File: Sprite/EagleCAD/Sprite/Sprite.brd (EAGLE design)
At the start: 35 x 35 mm, 29 parts, among them U1 CC430F5137, U2 HMC5883LSMD, U3 ITG-3200, X1 26 MHz

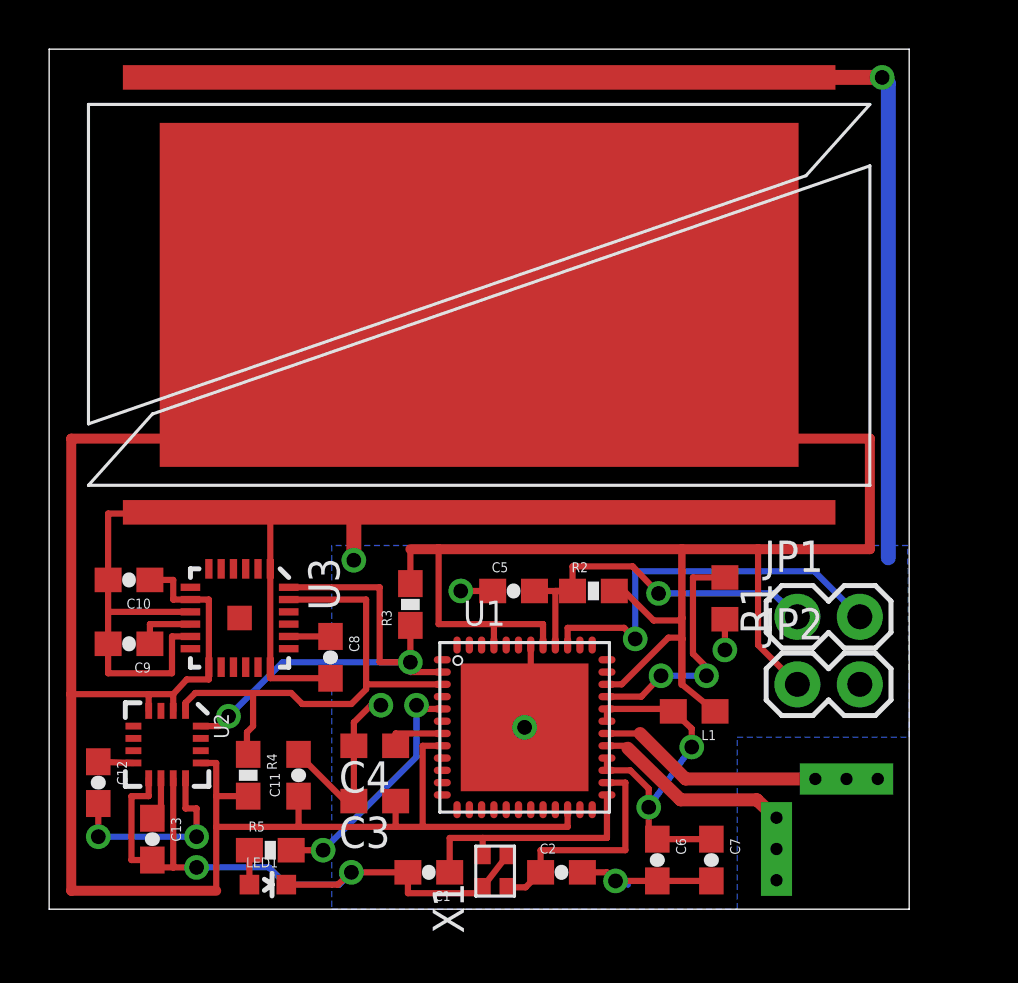
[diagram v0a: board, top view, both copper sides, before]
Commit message: Added back solar cells and TCXO to Sprite
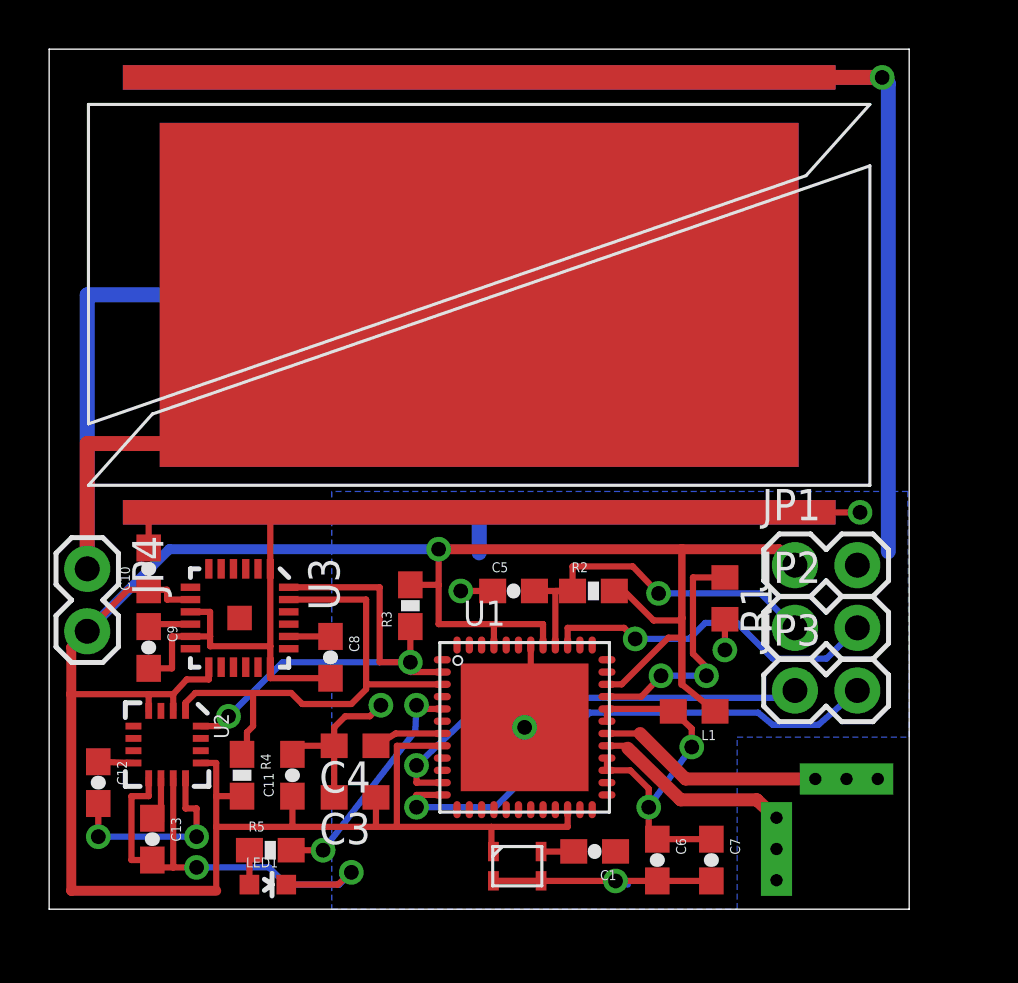
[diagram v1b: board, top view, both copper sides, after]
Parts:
- removed C2: 27pF, SparkFun:0603-CAP
- removed X1: 26 MHz, ABM11:ABM11_CERAMIC-SMD-CRYSTAL
- added JP3, JP4: (no value), SparkFun:1X02
- added S2: TASC, TASC:TASC
- added U$1: TCXO_7Z, SpriteTCXO:TXC_7Z
- C1: value 27pF -> 10 nF
- moved C1 6.80 mm to (22.2, 2.35)
- moved JP2 2.30 mm to (30.4, 11.4)
- moved JP1 2.10 mm to (30.4, 14.0)
- moved C10 0.92 mm to (4.05, 13.8), turned to 90 degrees
- moved C3 0.81 mm to (12.4, 4.55)
- moved C9 0.81 mm to (4.05, 10.7), turned to 270 degrees
- moved C4 0.80 mm to (12.4, 6.65)
- moved C11 0.25 mm to (9.90, 5.45)
- moved R4 0.25 mm to (7.85, 5.45)
- moved R3 0.05 mm to (14.7, 12.3)
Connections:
- removed net N$2: C1.1, U1.25, X1.P$1
- new net N$12: C1.2, U$1.OUT
- new net RXD: JP3.2, U1.12
- new net TXD: JP3.1, U1.11
- new net VSOLAR: JP4.1, S1.PLUS, S2.PLUS
- net GND: now also JP1.2, S2.MINUS1, S2.MINUS2, U$1.GND1, U$1.GND2; no longer C1.2, C2.2, JP2.2, X1.P$2, X1.P$4
- net N$1: now also C1.1, U1.25; no longer C2.1, U1.26, X1.P$3
- net RST: now also JP2.1; no longer JP1.1
- net TEST: now also JP2.2; no longer JP1.2
- net VCC: now also JP1.1, JP4.2, U$1.VCC; no longer JP2.1, S1.PLUS
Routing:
- net VSOLAR: track 0.00 -> 54.2 mm
- net VCC: track 151.6 -> 115.3 mm, vias 0 -> 1
- net RXD: track 0.00 -> 21.8 mm, vias 0 -> 1
- net GND: track 130.1 -> 151.7 mm
- net TXD: track 0.00 -> 18.4 mm, vias 0 -> 1
- net N$2: track 10.2 -> 0.00 mm
- net N$1: track 9.44 -> 0.00 mm
- net TEST: track 16.3 -> 14.1 mm
- net N$12: track 0.00 -> 1.34 mm
- net N$9: track 2.45 -> 1.76 mm

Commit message: New Sprite design
Several tweaks to the Sprite on the way to the flight unit. Added pins
and holes to interface to the deployer as well as a TCXO.
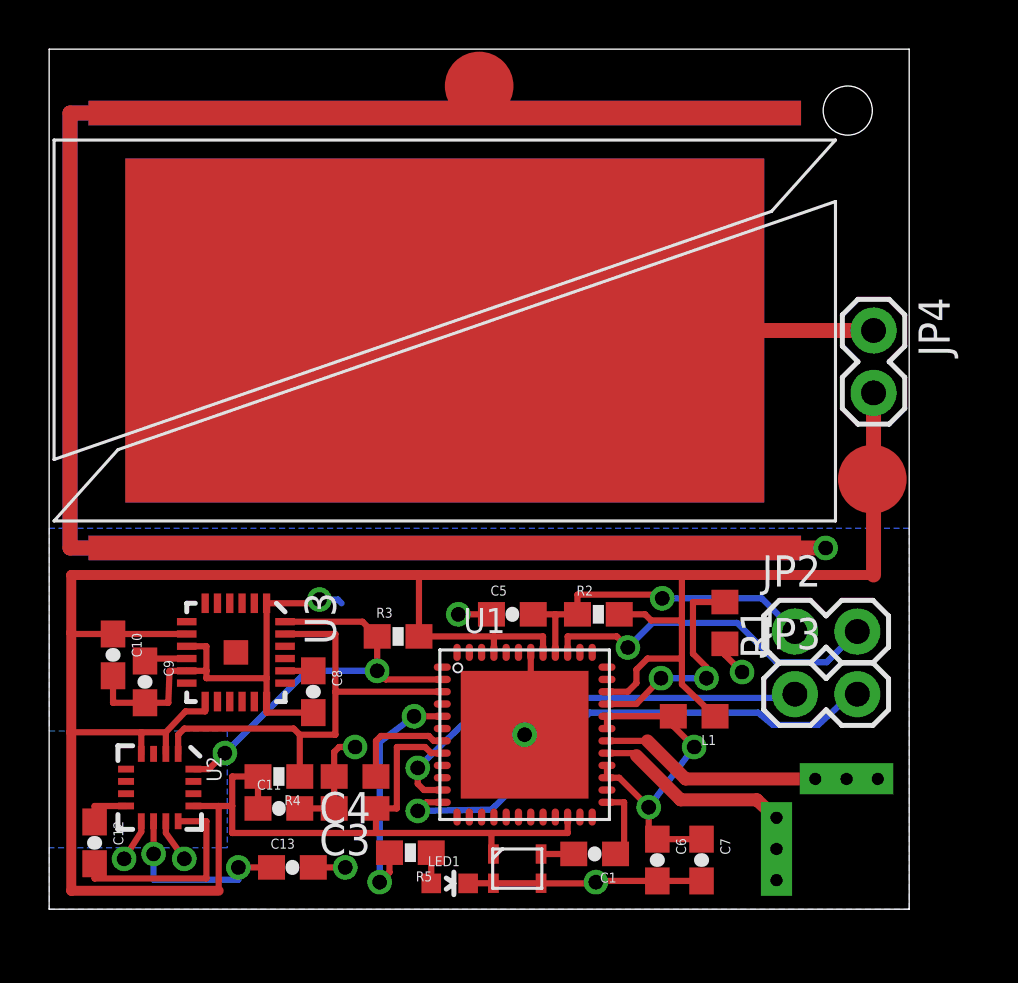
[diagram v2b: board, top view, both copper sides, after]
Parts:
- removed JP1: (no value), SparkFun:1X02
- added P1, P2: SPRITE_PIN, SpritePin:SPRITE_PIN
- C6: value 100nF -> 10nF
- C7: value 10nF -> 100nF
- moved JP4 33.4 mm to (33.5, 23.6)
- moved LED1 7.40 mm to (16.3, 1.05)
- moved C13 5.81 mm to (9.90, 1.70), turned to 0 degrees
- moved R5 5.70 mm to (14.7, 2.30), turned to 180 degrees
- moved C10 3.79 mm to (2.60, 10.3), turned to 270 degrees
- moved C12 2.45 mm to (1.85, 2.70)
- moved S1 2.02 mm to (0.20, 15.8)
- moved S2 2.02 mm to (32.0, 15.8)
- moved U2 1.78 mm to (4.50, 4.95)
- moved C8 1.57 mm to (10.8, 8.85)
- moved R4 1.50 mm to (9.35, 5.40), turned to 180 degrees
- moved C11 1.46 mm to (9.35, 4.10), turned to 0 degrees
- moved C9 1.41 mm to (3.90, 9.25)
- moved U3 1.41 mm to (7.60, 10.4)
- moved R3 1.35 mm to (14.2, 11.1), turned to 0 degrees
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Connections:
- net GND: no longer JP1.2
- net VCC: no longer JP1.1
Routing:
- net VSOLAR: track 54.2 -> 34.9 mm
- net VCC: track 115.3 -> 124.5 mm, vias 1 -> 0
- net GND: track 151.7 -> 157.4 mm, vias 9 -> 10
- net N$7: track 2.16 -> 7.68 mm, vias 0 -> 2
- net SDA: track 20.8 -> 17.3 mm
- net N$1: track 0.00 -> 3.06 mm
- net RST: track 15.6 -> 13.6 mm
- net VCCRF: track 15.9 -> 14.1 mm
- net N$4: track 2.84 -> 4.32 mm
- net SCL: track 21.0 -> 19.6 mm
- net N$3: track 9.95 -> 9.13 mm
- net N$8: track 1.95 -> 1.15 mm
- net N$6: track 8.18 -> 8.63 mm, vias 2 -> 0

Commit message: Tightened up spacing between tasc cells and ground pads
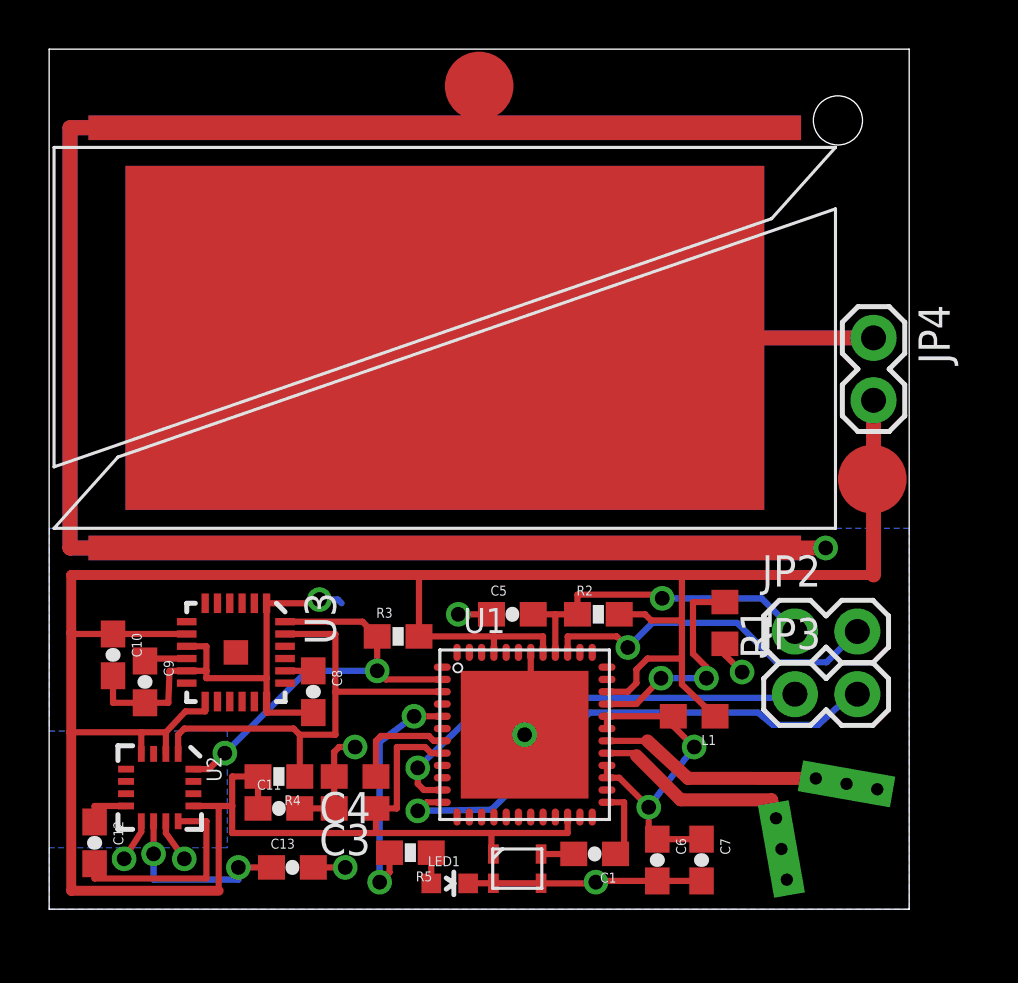
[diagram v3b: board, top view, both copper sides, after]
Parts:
- moved JP4 0.30 mm to (33.5, 23.2)
- moved S1 0.30 mm to (0.20, 15.5)
- moved S2 0.30 mm to (32.0, 15.5)
- moved ANT-N 0.20 mm to (32.5, 5.10), turned to 170 degrees
- moved ANT-P 0.20 mm to (29.8, 2.45), turned to 100 degrees
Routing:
- net GND: track 157.4 -> 156.2 mm
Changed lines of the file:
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@@
 <wire x1="35" y1="35" x2="0" y2="35" width="0" layer="20"/>
 <wire x1="0" y1="35" x2="0" y2="0" width="0" layer="20"/>
-<hole x="32.5" y="32.5" drill="2"/>
+<hole x="32.1" y="32.1" drill="2"/>
 </plain>
 <attributes>
@@
 <element name="R4" library="SparkFun" package="0603-RES" value="4.7K" x="9.35" y="5.4" rot="R180"/>
 <element name="JP2" library="SparkFun" package="1X02" value="" x="30.35" y="11.3"/>
-<element name="ANT-N" library="SpriteAntenna" package="ANTENNA" value="ANTENNA" x="32.45" y="5.3" rot="R180"/>
-<element name="ANT-P" library="SpriteAntenna" package="ANTENNA" value="ANTENNA" x="29.6" y="2.45" rot="R90"/>
+<element name="ANT-N" library="SpriteAntenna" package="ANTENNA" value="ANTENNA" x="32.45" y="5.1" rot="R170"/>
+<element name="ANT-P" library="SpriteAntenna" package="ANTENNA" value="ANTENNA" x="29.8" y="2.45" rot="R100"/>
 <element name="R2" library="SparkFun" package="0603-RES" value="47K" x="22.35" y="12"/>
 <element name="C5" library="SparkFun" package="0603-CAP" value="2.2nF" x="18.85" y="12"/>
@@
 <element name="LED1" library="SparkFun" package="LED-0603" value="" x="16.3" y="1.05" rot="R270"/>
 <element name="R5" library="SparkFun" package="0603-RES" value="270R" x="14.7" y="2.3" rot="R180"/>
-<element name="JP4" library="SparkFun" package="1X02" value="" x="33.55" y="23.55" rot="R270"/>
+<element name="JP4" library="SparkFun" package="1X02" value="" x="33.55" y="23.25" rot="R270"/>
 <element name="JP3" library="SparkFun" package="1X02" value="" x="30.35" y="8.75"/>
-<element name="S2" library="TASC" package="TASC" value="TASC" x="32" y="15.8" rot="MR0"/>
+<element name="S2" library="TASC" package="TASC" value="TASC" x="32" y="15.5" rot="MR0"/>
 <element name="U$1" library="SpriteTCXO" package="TXC_7Z" value="TCXO_7Z" x="19.05" y="1.65"/>
 <element name="P2" library="SpritePin" package="SPRITE_PIN" value="SPRITE_PIN" x="17.5" y="33.5"/>
 <element name="P1" library="SpritePin" package="SPRITE_PIN" value="SPRITE_PIN" x="33.5" y="17.5"/>
-<element name="S1" library="TASC" package="TASC" value="TASC" x="0.2" y="15.8"/>
+<element name="S1" library="TASC" package="TASC" value="TASC" x="0.2" y="15.5"/>
 </elements>
 <signals>
@@
 <wire x1="18.08" y1="2.245" x2="18" y2="2.345" width="0.254" layer="1"/>
 <wire x1="18" y1="2.345" x2="18" y2="3.1" width="0.254" layer="1"/>
-<wire x1="33.55" y1="21.01" x2="33.55" y2="13.6" width="0.6096" layer="1"/>
+<wire x1="33.55" y1="20.71" x2="33.55" y2="13.6" width="0.6096" layer="1"/>
 <wire x1="25.75" y1="11.75" x2="25.75" y2="13.5" width="0.254" layer="1"/>
 <wire x1="24.5" y1="11.75" x2="24.25" y2="12" width="0.254" layer="1"/>
@@
 <contactref element="S1" pad="MINUS2"/>
 <contactref element="S1" pad="MINUS1"/>
-<wire x1="16.1" y1="32.4" x2="0.85" y2="32.4" width="0.6096" layer="16"/>
-<wire x1="0.85" y1="32.4" x2="0.85" y2="14.7" width="0.6096" layer="16"/>
+<wire x1="16.1" y1="31.8" x2="0.85" y2="31.8" width="0.6096" layer="16"/>
+<wire x1="0.85" y1="31.8" x2="0.85" y2="14.7" width="0.6096" layer="16"/>
 <wire x1="0.85" y1="14.7" x2="16.1" y2="14.7" width="0.6096" layer="16"/>
-<wire x1="16.1" y1="32.4" x2="0.85" y2="32.4" width="0.6096" layer="1"/>
-<wire x1="0.85" y1="32.4" x2="0.85" y2="14.7" width="0.6096" layer="1"/>
+<wire x1="16.1" y1="31.8" x2="0.85" y2="31.8" width="0.6096" layer="1"/>
+<wire x1="0.85" y1="31.8" x2="0.85" y2="14.7" width="0.6096" layer="1"/>
 <wire x1="0.85" y1="14.7" x2="16.1" y2="14.7" width="0.6096" layer="1"/>
 <wire x1="27.5" y1="10.8" x2="27.5" y2="10.35" width="0.254" layer="1"/>
@@
 <contactref element="ANT-N" pad="IN3"/>
 <contactref element="ANT-N" pad="IN2"/>
-<wire x1="32.45" y1="5.3" x2="33.72" y2="5.3" width="0.53" layer="1"/>
-<wire x1="31.18" y1="5.3" x2="32.45" y2="5.3" width="0.53" layer="1"/>
-<wire x1="25.9" y1="5.3" x2="31.18" y2="5.3" width="0.53" layer="1"/>
+<wire x1="32.45" y1="5.1" x2="33.700703125" y2="4.879465625" width="0.53" layer="1"/>
+<wire x1="31.19929375" y1="5.32053125" x2="32.45" y2="5.1" width="0.53" layer="1"/>
+<wire x1="26" y1="5.325" x2="31.19929375" y2="5.32053125" width="0.53" layer="1"/>
 <wire x1="22.7" y1="6.85" x2="24.35" y2="6.85" width="0.254" layer="1"/>
-<wire x1="24.35" y1="6.85" x2="25.9" y2="5.3" width="0.53" layer="1"/>
+<wire x1="24.35" y1="6.85" x2="26" y2="5.325" width="0.53" layer="1"/>
 </signal>
 <signal name="RFP">
@@
 <contactref element="ANT-P" pad="IN3"/>
 <contactref element="ANT-P" pad="IN2"/>
-<wire x1="29.6" y1="2.45" x2="29.6" y2="3.7" width="0.53" layer="1"/>
-<wire x1="29.6" y1="3.7" x2="29.6" y2="3.72" width="0.254" layer="1"/>
-<wire x1="29.6" y1="1.18" x2="29.6" y2="2.45" width="0.53" layer="1"/>
+<wire x1="30.02053125" y1="1.19929375" x2="29.8" y2="2.45" width="0.53" layer="1"/>
 <wire x1="23.9" y1="6.25" x2="25.7" y2="4.45" width="0.53" layer="1"/>
-<wire x1="25.7" y1="4.45" x2="28.8" y2="4.45" width="0.53" layer="1"/>
-<wire x1="28.8" y1="4.45" x2="29.6" y2="3.7" width="0.53" layer="1"/>
+<wire x1="25.7" y1="4.45" x2="29.4" y2="4.45" width="0.53" layer="1"/>
 <wire x1="22.7" y1="6.35" x2="23.75" y2="6.35" width="0.254" layer="1"/>
 <wire x1="23.75" y1="6.35" x2="23.9" y2="6.25" width="0.254" layer="1"/>
+<wire x1="29.8" y1="2.45" x2="29.579465625" y2="3.700703125" width="0.53" layer="1"/>
+<wire x1="29.579465625" y1="3.700703125" x2="29.4" y2="4.45" width="0.53" layer="1"/>
 </signal>
 <signal name="RST">
@@
 <contactref element="S2" pad="PLUS"/>
 <contactref element="S1" pad="PLUS"/>
-<wire x1="33.55" y1="23.55" x2="16.1" y2="23.55" width="0.6096" layer="1"/>
-<wire x1="16.1" y1="23.55" x2="33.55" y2="23.55" width="0.6096" layer="16"/>
+<wire x1="33.55" y1="23.25" x2="16.1" y2="23.25" width="0.6096" layer="1"/>
+<wire x1="16.1" y1="23.25" x2="33.55" y2="23.25" width="0.6096" layer="16"/>
 </signal>
 <signal name="TXD">
